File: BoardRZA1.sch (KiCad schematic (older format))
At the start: 158 parts, among them CON1 USB-MINI-B, CON2 USB-A-PCB, CON3 con-microSD, CON4 BARREL_JACK, J1 HR911105A, J2 SIL38, P1 CONN_5X2, SW1 RESET, SW2 NMI, SW3 SW0, SW4 SW1, U1 RZ-A1L, U2 13MHz, U3 48MHz, U4 N25QXXX, U5 AS4C16M16S, U6 BA3259HFP, U7 BU42xx, U8 KSZ8041MLL, U9 25MHz, X1 32.768k

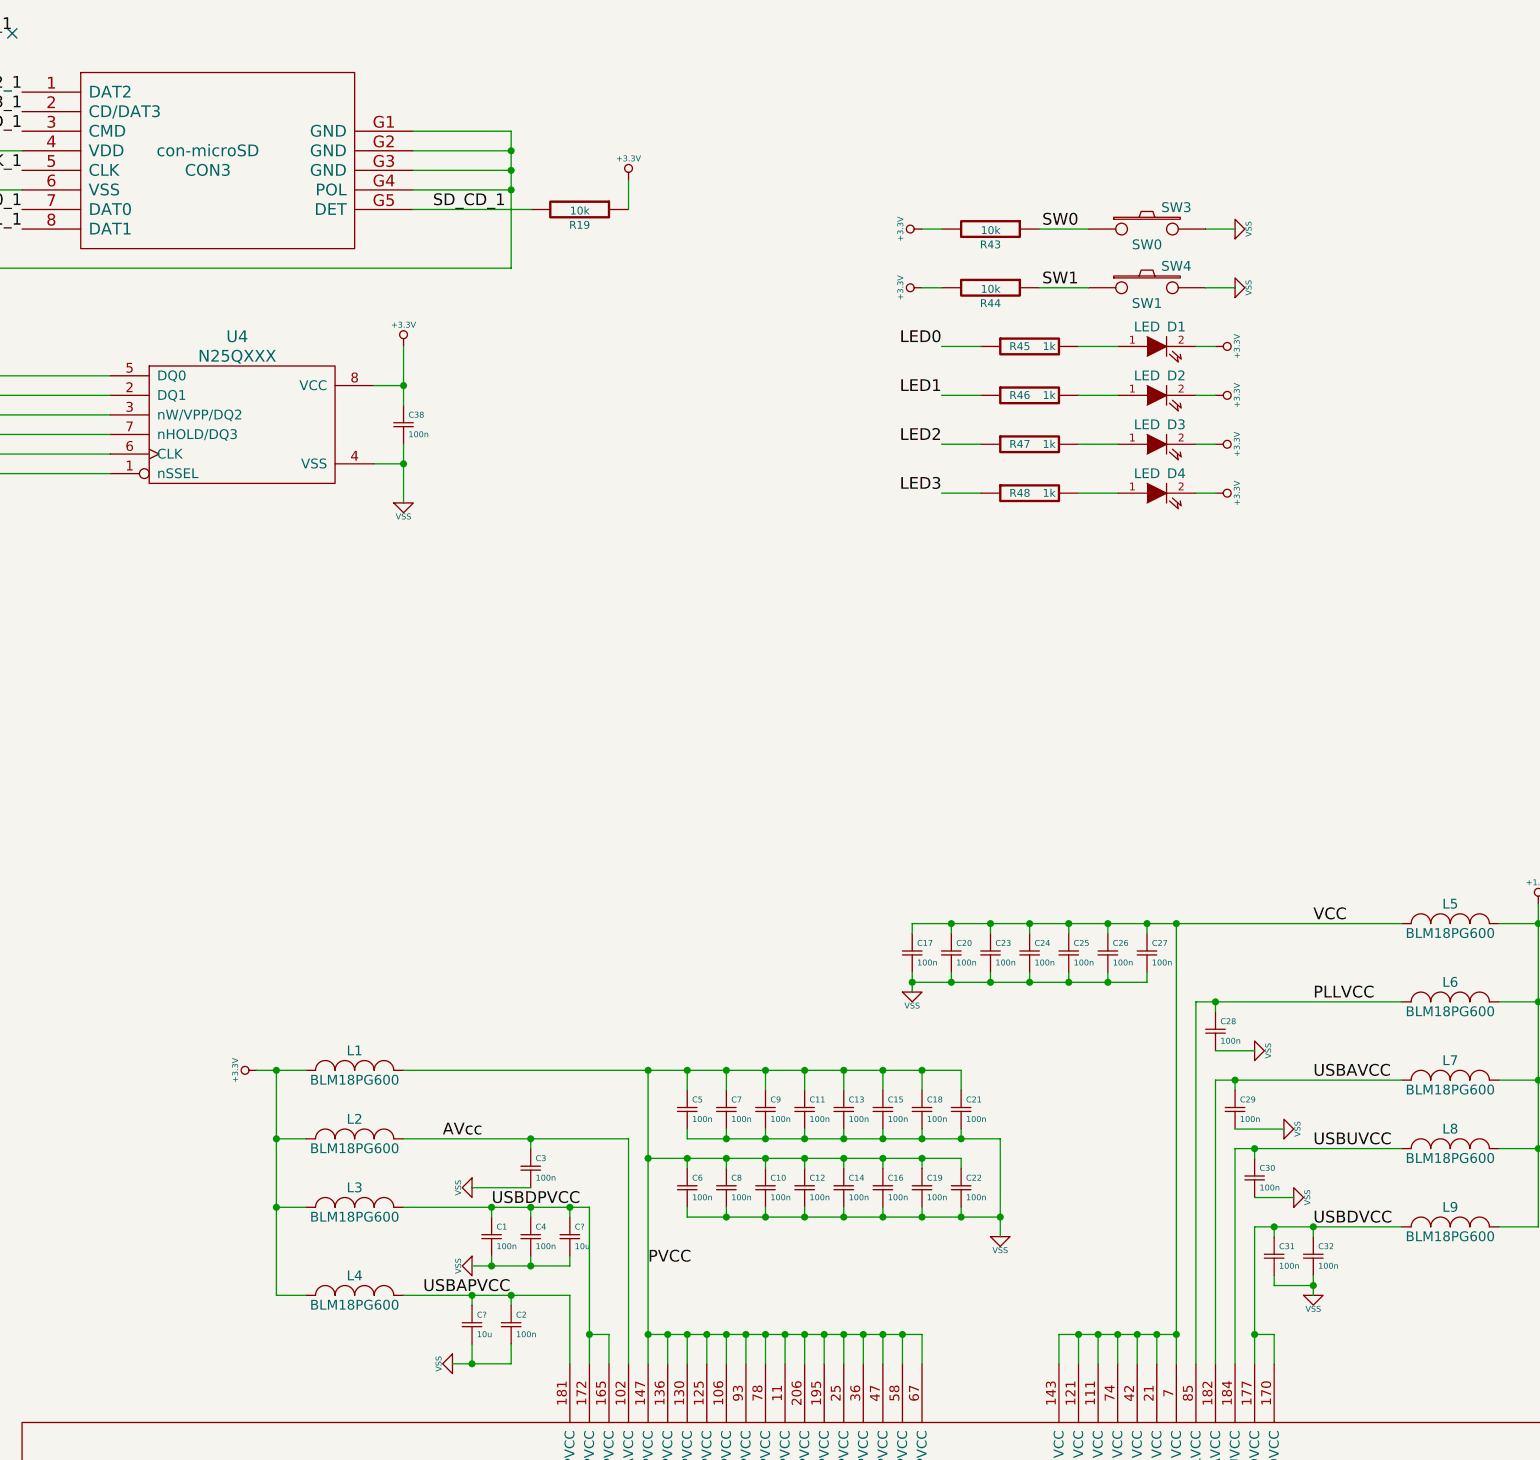
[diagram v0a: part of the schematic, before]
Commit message: Add 10uF decouple on pvcc, vcc & 3v3
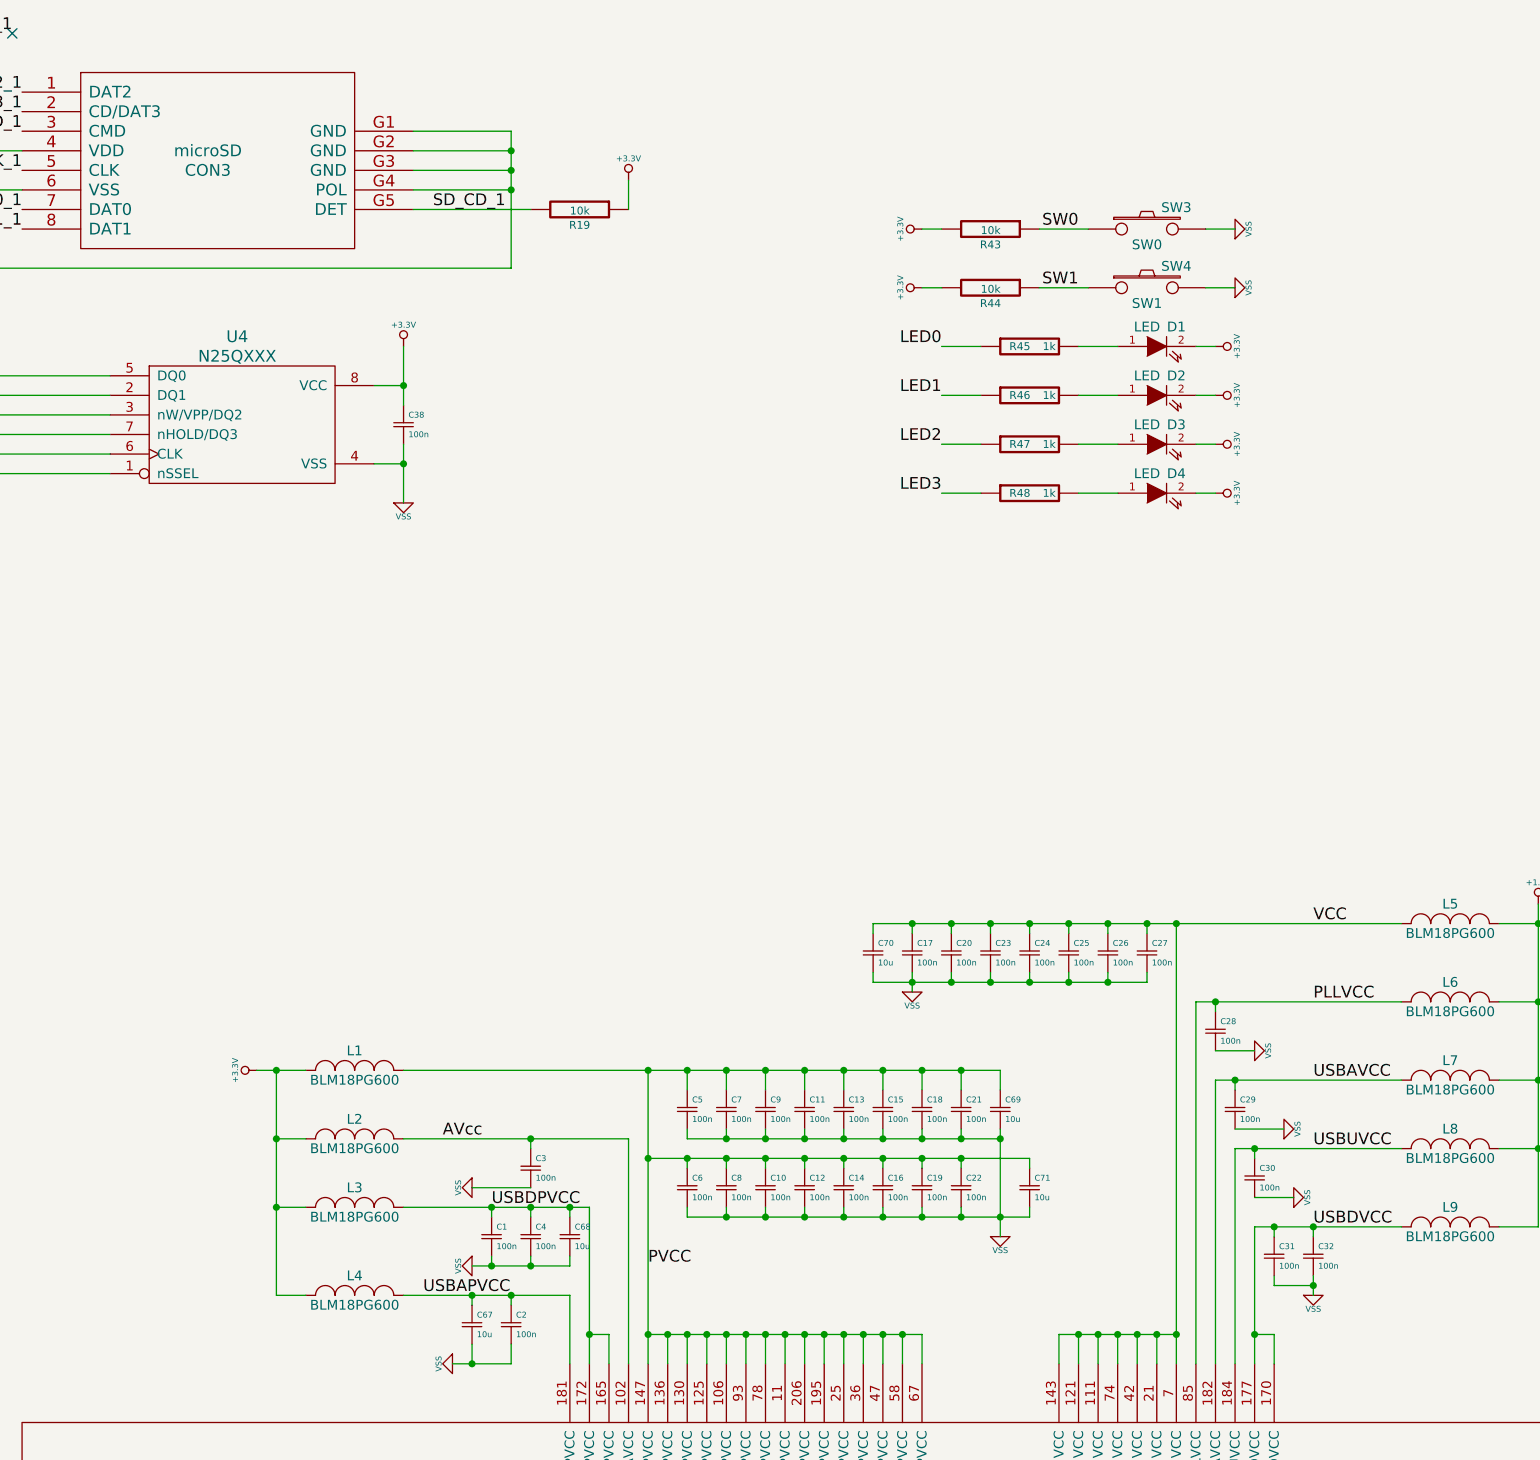
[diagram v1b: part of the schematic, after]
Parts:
- added C69, C70, C71: 10u, SMD_Packages:SM0805, symbol Csmall
- CON3: value con-microSD -> microSD
- gave numbers to parts that had none: 2
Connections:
- net PVCC: now also C69.1, C71.1
- net VCC: now also C70.1
- net VSS: now also C69.2, C70.2, C71.2

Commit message: Add 100pF C over power rails (700MHz filters) ERC pass DRC pass
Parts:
- added C72, C73, C74, C75, C76: 100p, SMD_Packages:SM0805, symbol Csmall
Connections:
- net +3.3V: now also C72.1
- net PLLVCC: now also C76.1
- net PVCC: now also C73.1, C74.1
- net VCC: now also C75.1
- net VSS: now also C72.2, C73.2, C74.2, C75.2, C76.2
- no-connect marks 13 -> 17

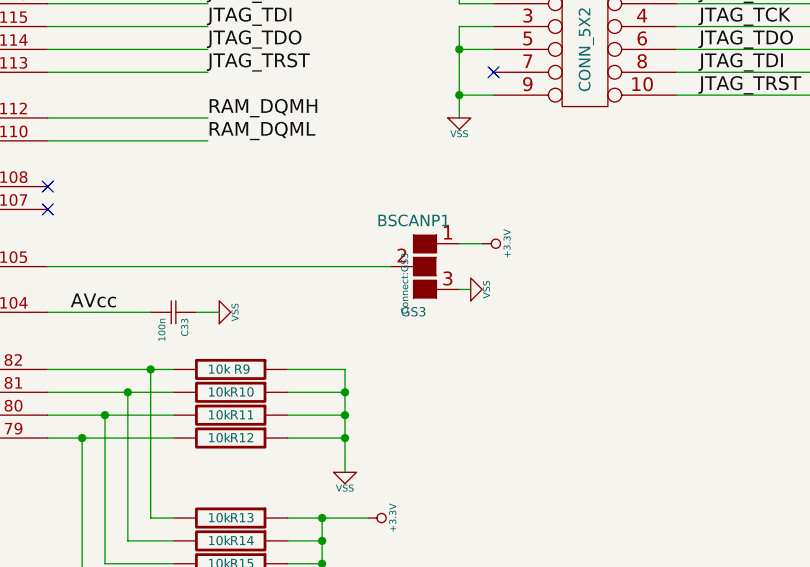
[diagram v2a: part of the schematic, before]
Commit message: Correct U4 SOP2-8 package. Rearangue footprint libraries
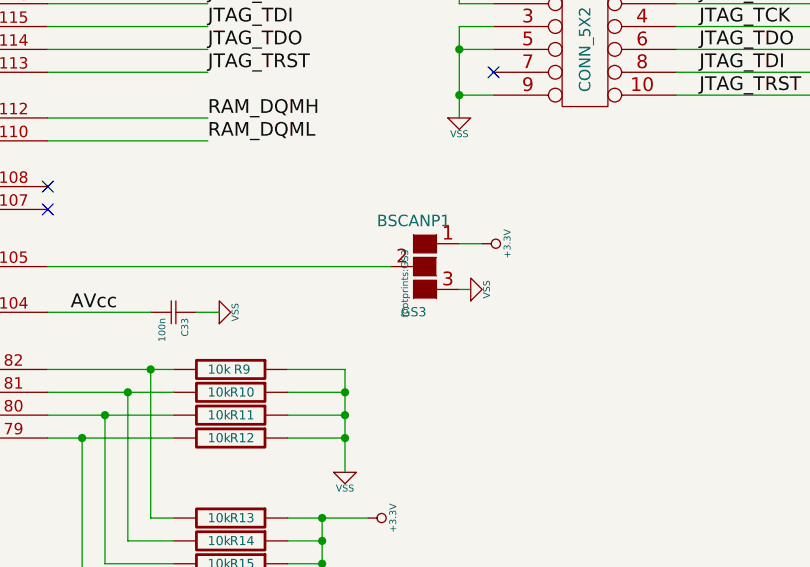
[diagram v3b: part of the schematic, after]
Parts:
- BSCANP1: footprint Connect:GS3 -> footprints:GS3
- C1, C10, C11, C12, C13, C14, C15, C16, C17, C18, C19, C2, C20, C21, C22, C23, C24, C25, C26, C27, C28, C29, C3, C30, C31, C32, C33, C34, C35, C36, C37, C38, C39, C4, C40, C41, C42, C43, C44, C45, C46, C5, C52, C53, C54, C55, C56, C57, C58, C59, C6, C60, C61, C62, C63, C64, C65, C66, C67, C68, C69, C7, C70, C71, C72, C73, C74, C75, C76, C8, C9, L1, L10, L2, L3, L4, L5, L6, L7, L8, L9, R1, R10, R11, R12, R13, R14, R15, R16, R17, R18, R19, R2, R20, R21, R22, R23, R24, R25, R26, R27, R28, R29, R3, R30, R31, R32, R33, R34, R35, R36, R37, R38, R39, R4, R40, R41, R42, R43, R44, R45, R46, R47, R48, R49, R5, R50, R51, R6, R7, R8, R9: footprint SMD_Packages:SM0805 -> footprints:SM0805
- C47, C48, C49, C50, C51: footprint Capacitors_SMD:c_0805 -> footprints:c_0805
- CON1: footprint Connect:USB_MINI_B -> footprints:USB_MINI_B
- CON2: footprint Connect:USB_A -> footprints:USB_A
- CON3: footprint microsd:microSD -> footprints:microSD
- CON4: footprint Connect:BARREL_JACK -> footprints:BARREL_JACK
- D1, D2, D3, D4, D7: footprint LEDs:LED-0805 -> footprints:LED-0805
- D5, D6: footprint Diodes_SMD:Diode-SMA_Standard -> footprints:Diode-SMA_Standard
- J1: footprint RJ45:RJ45_Pulse_J403-A -> footprints:RJ45_Pulse_J403-A
- J2: footprint Pin_Headers:Pin_Header_Angled_1x38 -> footprints:Pin_Header_Angled_1x38
- P1: footprint Connect:VASCH5x2 -> footprints:VASCH5x2
- SW1, SW2, SW3, SW4: footprint PushButton:RigthAnglePush -> footprints:RigthAnglePush
- U1: footprint SMD_Packages:PQFP208 -> footprints:PQFP208
- U2: footprint OSC_4PIN:OSC_2x2p5 -> footprints:OSC_2x2p5
- U3, U9: footprint OSC_4PIN:OSC_4PIN -> footprints:OSC_4PIN
- U4: footprint SMD_Packages:MSOP_8 -> footprints:SOP2-8
- U5: footprint TSOP_II_54:TSOP_II_54 -> footprints:TSOP_II_54
- U6: footprint Rohm:Rohm-HRP5 -> footprints:Rohm-HRP5
- U7: footprint Rohm:SSOP-5 -> footprints:SSOP-5
- U8: footprint smd_qfp:LQFP48-M05 -> footprints:LQFP48-M05
- X1: footprint Crystals:Crystal_Round_Vertical_3mm -> footprints:Crystal_Round_Vertical_3mm

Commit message: Add testpoints
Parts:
- added P10, P11, P12, P13, P14, P15, P16, P17, P2, P3, P4, P5, P6, P7, P8, P9: CONN_1, Connect:PINTST, symbol CONN_1
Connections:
- net +1.2V: now also P9.1
- net +3.3V: now also P6.1
- net +5v: now also P2.1
- net PVCC: now also P7.1
- net RAM_CLK: now also P5.1
- net USB_CLK: now also P3.1
- net VCC: now also P8.1
- net VSS: now also P10.1, P11.1, P12.1, P13.1, P14.1, P15.1, P16.1, P17.1
- net at R2.1, U1.86 (EXTAL): now also P4.1

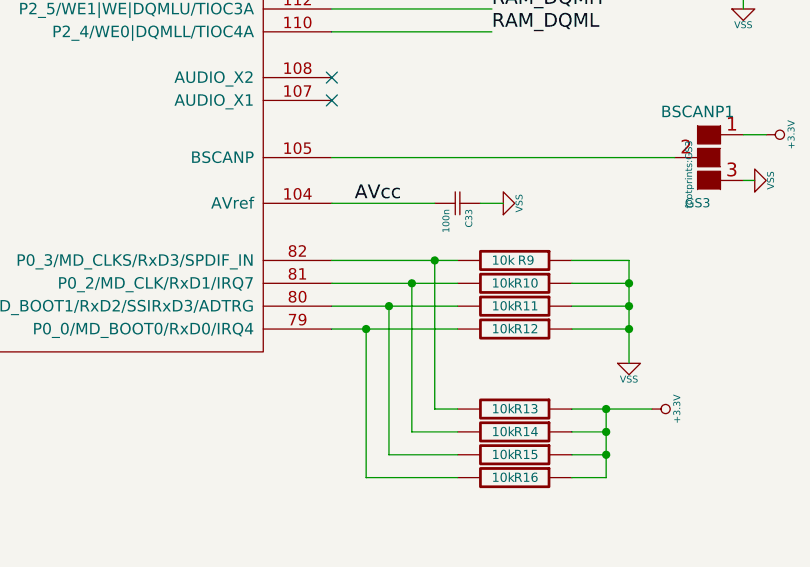
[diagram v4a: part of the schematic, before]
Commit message: Arrange Sylkscreen
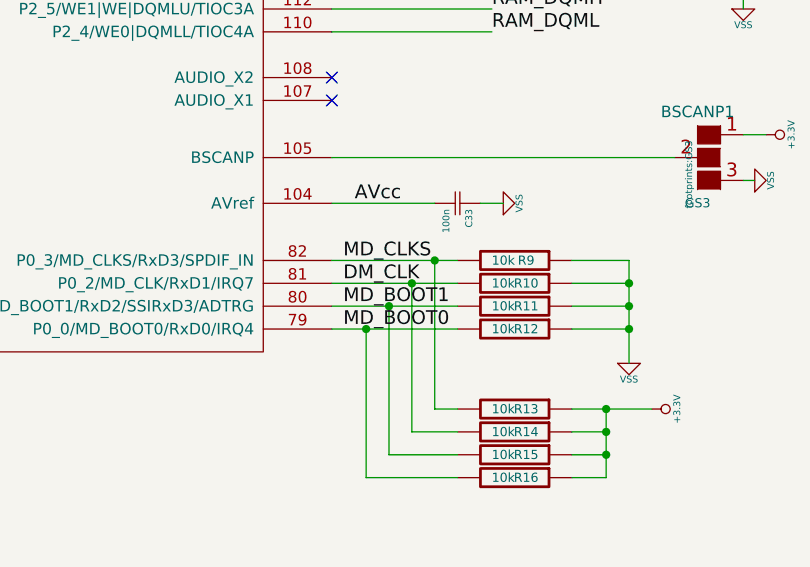
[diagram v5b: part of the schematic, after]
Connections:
- net MD_BOOT0: now reaches R12.2, R16.2, U1.79 (P0_0/MD_BOOT0/RxD0/IRQ4)
- net MD_BOOT1: now reaches R11.2, R15.2, U1.80 (P0_1/MD_BOOT1/RxD2/SSIRxD3/ADTRG)
- net DM_CLK: now reaches R10.2, R14.2, U1.81 (P0_2/MD_CLK/RxD1/IRQ7)
- net MD_CLKS: now reaches R13.2, R9.2, U1.82 (P0_3/MD_CLKS/RxD3/SPDIF_IN)
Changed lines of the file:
@@
 Text Label 17350 6300 2    60   ~ 0
 RAM_CLK
+Text Label 28000 17150 0    60   ~ 0
+MD_CLKS
+Text Label 28000 17250 0    60   ~ 0
+DM_CLK
+Text Label 28000 17350 0    60   ~ 0
+MD_BOOT1
+Text Label 28000 17450 0    60   ~ 0
+MD_BOOT0
 $EndSCHEMATC

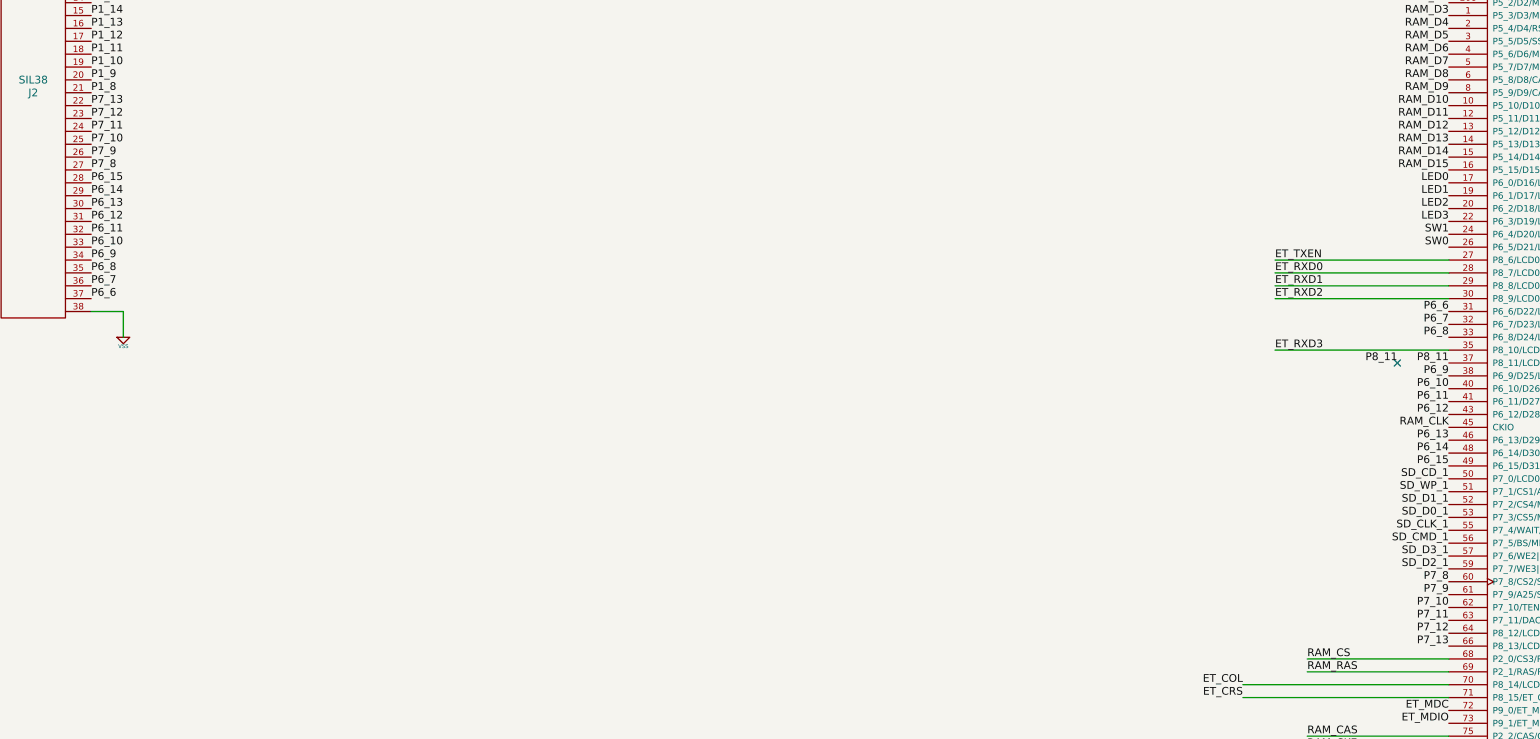
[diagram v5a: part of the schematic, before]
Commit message: Add serial connector over UART4. Add GPIO labels, update images
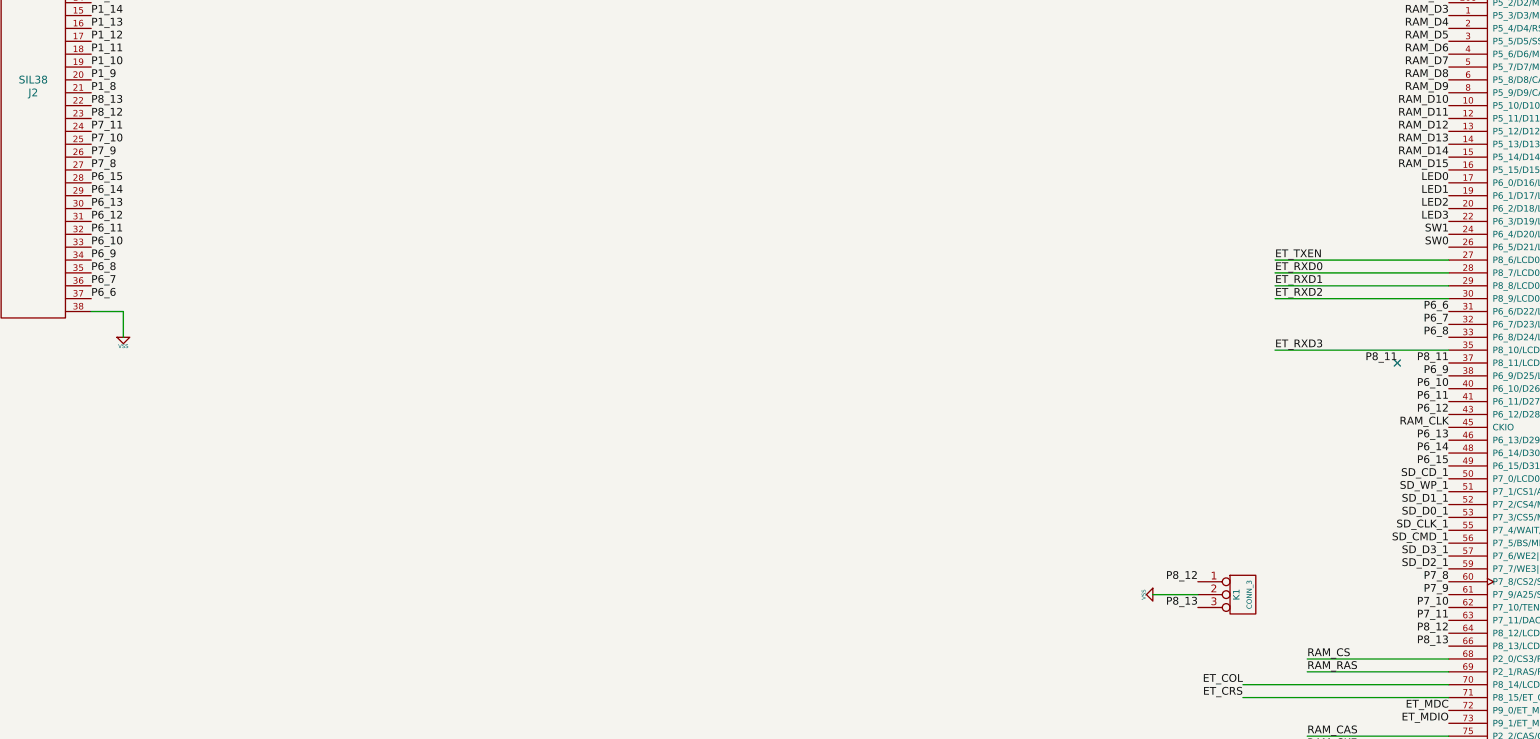
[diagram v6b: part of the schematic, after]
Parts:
- added K1: CONN_3, Connect:SIL-3, symbol CONN_3
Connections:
- net VSS: now also K1.2 (PM)
- net P7_12 renamed P8_12
- net P8_12: now also K1.1 (P1)
- net P7_13 renamed P8_13
- net P8_13: now also K1.3 (P3)
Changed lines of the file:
@@
 P7_11
 Text Label 18650 14450 2    60   ~ 0
-P7_12
+P8_12
 Text Label 18650 14550 2    60   ~ 0
-P7_13
+P8_13
 Text Label 8100 10850 0    60   ~ 0
 P7_8
@@
 Text Label 8100 10550 0    60   ~ 0
 P7_11
-Text Label 8100 10450 0    60   ~ 0
-P7_12
-Text Label 8100 10350 0    60   ~ 0
-P7_13
 Text Label 18650 11950 2    60   ~ 0
 P6_6
@@
 F 3 "" H 34700 1600 60  0000 C CNN
 	1    34700 1600
-	1    0    0    -1
+	1    0    0    1
 $EndComp
 $Comp
@@
 Text Label 28000 17450 0    60   ~ 0
 MD_BOOT0
+Text Label 8100 10450 0    60   ~ 0
+P8_12
+Text Label 8100 10350 0    60   ~ 0
+P8_13
+Text Label 16700 14050 2    60   ~ 0
+P8_12
+Text Label 16700 14250 2    60   ~ 0
+P8_13
+$Comp
+L VSS #PWR082
+U 1 1 54919CCD
+P 16350 14150
+F 0 "#PWR082" H 16350 14150 30  0001 C CNN
+F 1 "VSS" H 16350 14080 30  0000 C CNN
+F 2 "" H 16350 14150 60  0000 C CNN
+F 3 "" H 16350 14150 60  0000 C CNN
+	1    16350 14150
+	0    1    1    0
+$EndComp
+$Comp
+L CONN_3 K1
+U 1 1 5490F5C6
+P 17050 14150
+F 0 "K1" V 17000 14150 50  0000 C CNN
+F 1 "CONN_3" V 17100 14150 40  0000 C CNN
+F 2 "Connect:SIL-3" H 17050 14150 60  0001 C CNN
+F 3 "" H 17050 14150 60  0000 C CNN
+	1    17050 14150
+	1    0    0    -1
+$EndComp
+Wire Wire Line
+	16350 14150 16700 14150
 $EndSCHEMATC
